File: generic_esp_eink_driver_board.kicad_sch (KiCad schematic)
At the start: 53 parts, among them IC1 TPS7A0233PDBVR, IC2 MAX17260SETD+T, J1 USB_C_Receptacle_USB2.0_16P, J2 S2B-PH-SM4-TB, J3 Conn_01x04, Q1 AO3400A, U1 USBLC6-2SC6, U2 BQ24040DSQR, U3 ESP32-S3-WROOM-1, U4 FPC24

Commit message: re-placement
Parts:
- added C21: 100nF, Capacitor_SMD:C_0805_2012Metric_Pad1.18x1.45mm_HandSolder, symbol Device:C
- added J4: Micro_SD_Card_Det_Hirose_DM3AT, Connector_Card:microSD_HC_Hirose_DM3AT-SF-PEJM5, symbol Connector:Micro_SD_Card_Det_Hirose_DM3AT
- added R13, R14, R15, R16, R17, R18: 10k, Resistor_SMD:R_0805_2012Metric_Pad1.20x1.40mm_HandSolder, symbol Device:R
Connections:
- net 3V3: now also C21.1, J4.4 (VDD), R13.1, R14.1, R15.1, R16.1, R17.1, R18.1
- net FG_SCL: now also U3.8 (IO15); no longer U3.9 (IO16)
- net FG_SDA: now also U3.9 (IO16); no longer U3.8 (IO15)
- net GND: now also C21.2, J4.6 (VSS), J4.9 (DET_B), J4.SH (SHIELD)
- net SD_D1: now reaches U3.24 (IO47)
- net SD_D1: now also J4.8 (DAT1), R18.2
- net SD_DET: now reaches U3.25 (IO48)
- net SD_DET: now also J4.10 (DET_A)
- net SD_D2: now reaches U3.31 (IO38)
- net SD_D2: now also J4.1 (DAT2), R13.2
- net at R7.1: now also U3.4 (IO4); no longer U3.32 (IO39)
- net SD_CMD: now reaches U3.33 (IO40)
- net SD_CMD: now also J4.3 (CMD), R15.2
- net SD_CLK: now reaches U3.34 (IO41)
- net SD_CLK: now also J4.5 (CLK), R16.2
- net SD_D0: now reaches U3.35 (IO42)
- net SD_D0: now also J4.7 (DAT0), R17.2
- new net SD_D3: J4.2 (DAT3/CD), R14.2, U3.32 (IO39)
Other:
- note added: "Battery EEMB 3.7V 820mAh 653042 Lipo Battery with JST Plug 2mm"
- note added: "Micro SD card"
- moved on the sheet: D3, R7

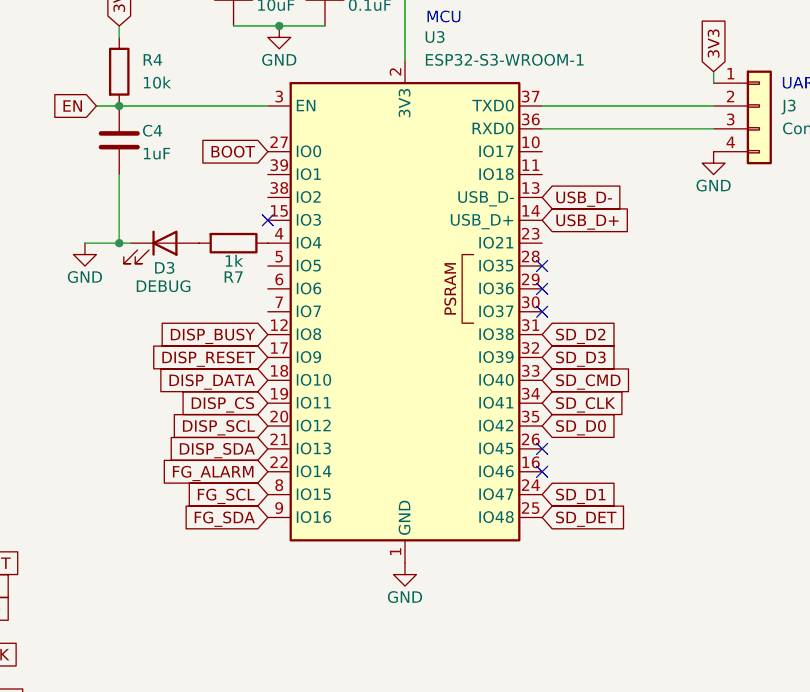
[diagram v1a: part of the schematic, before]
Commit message: Route SD card
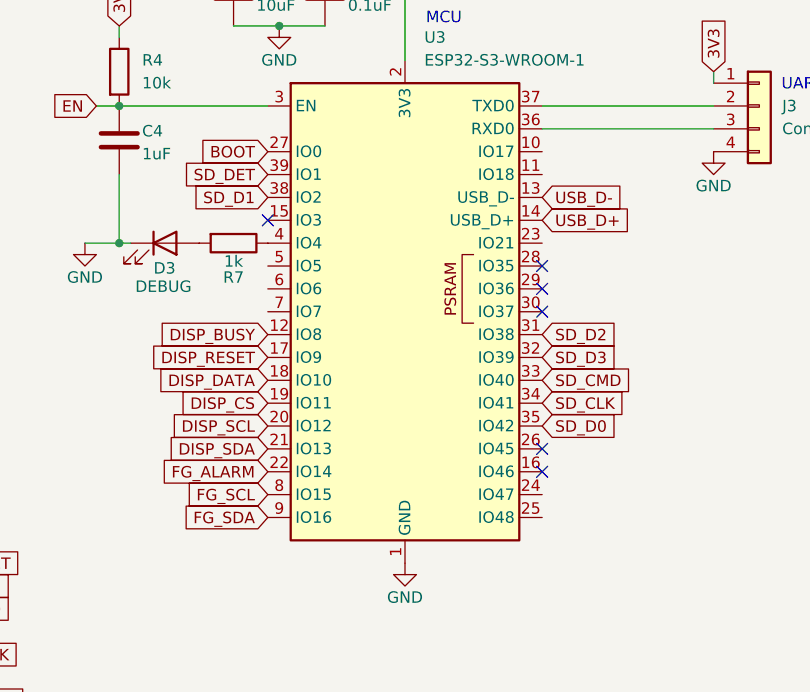
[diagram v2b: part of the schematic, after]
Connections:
- net SD_D1: now also U3.38 (IO2); no longer U3.24 (IO47)
- net SD_DET: now also U3.39 (IO1); no longer U3.25 (IO48)
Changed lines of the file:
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@@
 	(global_label "SD_DET"
 		(shape input)
-		(at 153.67 153.67 0)
-		(fields_autoplaced yes)
-		(effects
-			(font
-				(size 1.27 1.27)
-			)
-			(justify left)
-		)
-		(property "Intersheetrefs" "${INTERSHEET_REFS}"
-			(at 163.4889 153.67 0)
-			(hide yes)
-			(show_name no)
-			(do_not_autoplace no)
-			(effects
-				(font
-					(size 1.27 1.27)
-				)
-				(justify left)
+		(at 123.19 115.57 180)
+		(fields_autoplaced yes)
+		(effects
+			(font
+				(size 1.27 1.27)
+			)
+			(justify right)
+		)
+		(property "Intersheetrefs" "${INTERSHEET_REFS}"
+			(at 113.3711 115.57 0)
+			(hide yes)
+			(show_name no)
+			(do_not_autoplace no)
+			(effects
+				(font
+					(size 1.27 1.27)
+				)
+				(justify right)
 			)
 		)
@@
 	(global_label "SD_D1"
 		(shape input)
-		(at 153.67 151.13 0)
-		(fields_autoplaced yes)
-		(effects
-			(font
-				(size 1.27 1.27)
-			)
-			(justify left)
-		)
-		(property "Intersheetrefs" "${INTERSHEET_REFS}"
-			(at 162.5818 151.13 0)
-			(hide yes)
-			(show_name no)
-			(do_not_autoplace no)
-			(effects
-				(font
-					(size 1.27 1.27)
-				)
-				(justify left)
-			)
-		)
+		(at 123.19 118.11 180)
+		(fields_autoplaced yes)
+		(effects
+			(font
+				(size 1.27 1.27)
+			)
+			(justify right)
+		)
+		(property "Intersheetrefs" "${INTERSHEET_REFS}"
+			(at 114.2782 118.11 0)
+			(hide yes)
+			(show_name no)
+			(do_not_autoplace no)
+			(effects
+				(font
+					(size 1.27 1.27)
+				)
+				(justify right)
+			)
+		)

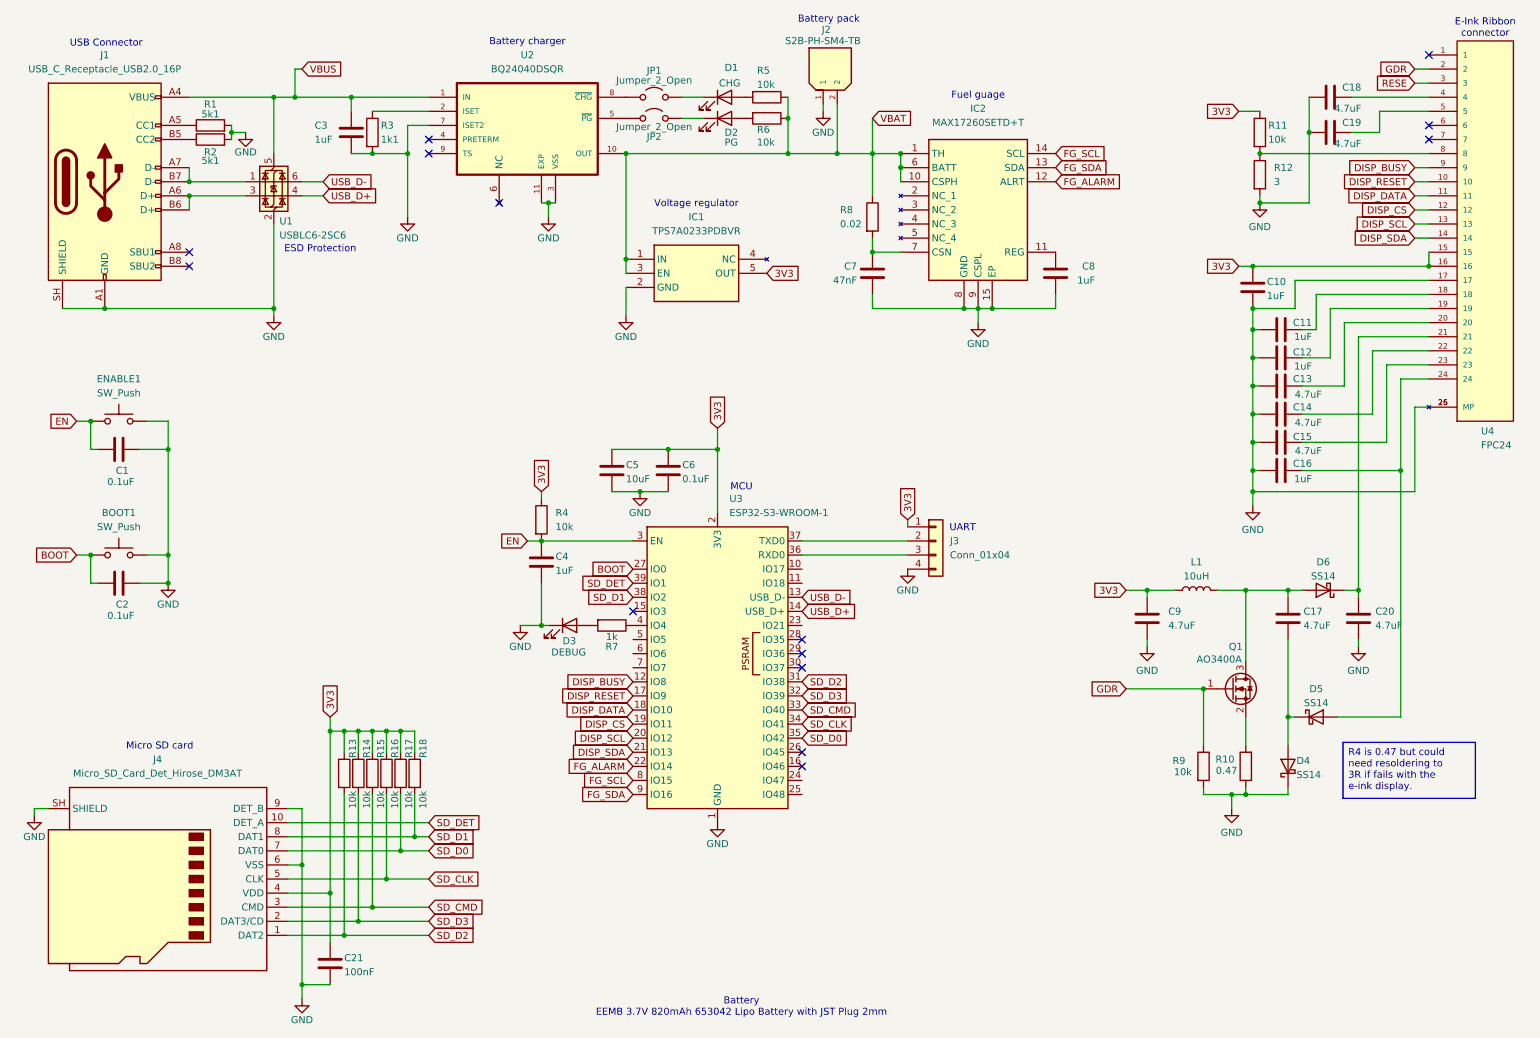
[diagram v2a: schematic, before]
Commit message: Add temp/hum sensor
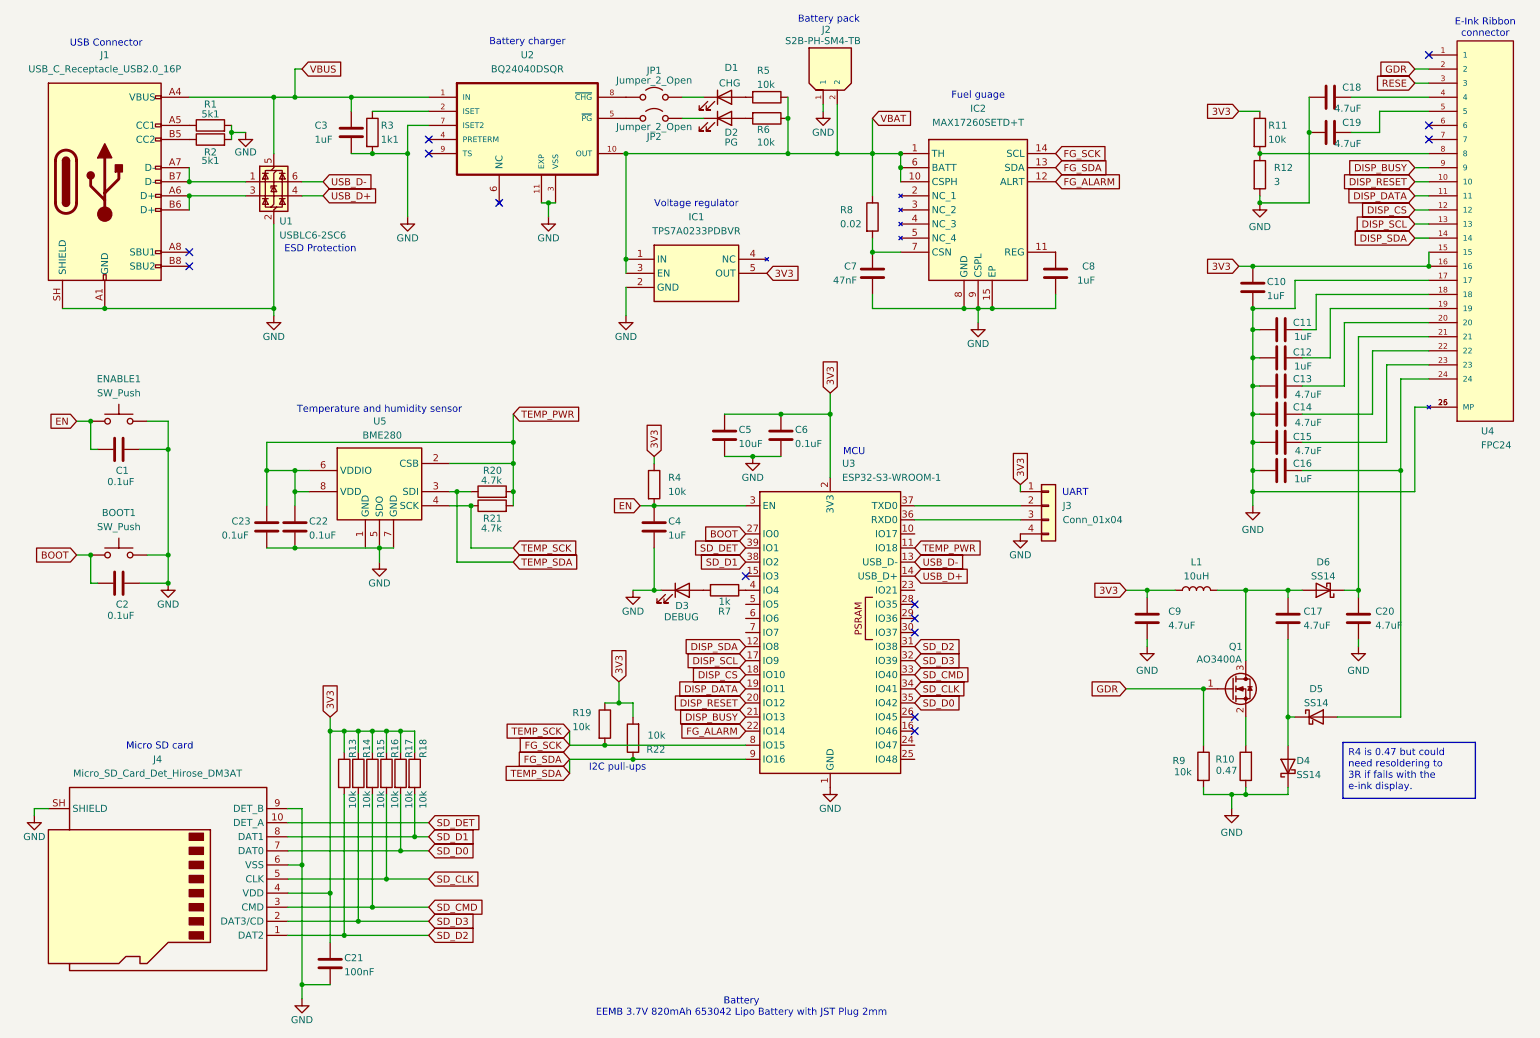
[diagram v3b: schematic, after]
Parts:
- added C22, C23: 0.1uF, Capacitor_SMD:C_0805_2012Metric_Pad1.18x1.45mm_HandSolder, symbol Device:C
- added R19, R22: 10k, Resistor_SMD:R_0805_2012Metric_Pad1.20x1.40mm_HandSolder, symbol Device:R
- added R20, R21: 4.7k, Resistor_SMD:R_0805_2012Metric_Pad1.20x1.40mm_HandSolder, symbol Device:R
- added U5: BME280, Package_LGA:Bosch_LGA-8_2.5x2.5mm_P0.65mm_ClockwisePinNumbering, symbol Sensor:BME280
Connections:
- net 3V3: now also R19.1, R22.2
- net DISP_BUSY: now also U3.21 (IO13); no longer U3.12 (IO8)
- net DISP_CS: now also U3.18 (IO10); no longer U3.19 (IO11)
- net DISP_DATA: now also U3.19 (IO11); no longer U3.18 (IO10)
- net DISP_RESET: now also U3.20 (IO12); no longer U3.17 (IO9)
- net DISP_SCL: now also U3.17 (IO9); no longer U3.20 (IO12)
- net DISP_SDA: now also U3.12 (IO8); no longer U3.21 (IO13)
- net FG_SDA: now also R20.1, R22.1, U5.3 (SDI)
- net GND: now also C22.2, C23.2, U5.5 (SDO), U5.7 (GND)
- net TEMP_PWR: now reaches U3.11 (IO18)
- net TEMP_PWR: now also C22.1, C23.1, R20.2, R21.2, U5.2 (CSB), U5.6 (VDDIO), U5.8 (VDD)
- net FG_SCL renamed FG_SCK
- net FG_SCK: now also R19.2, R21.1, U5.4 (SCK)
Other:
- note added: "I2C pull-ups"
- note added: "Temperature and humidity sensor"
- moved on the sheet: C4, C5, C6, D3, J3, R4, R7, U3
